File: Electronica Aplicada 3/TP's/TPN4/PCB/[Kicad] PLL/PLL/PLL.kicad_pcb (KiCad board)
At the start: 2 copper layers, 26 parts, among them J1 Alimentacion, J2 SeñalDeReferencia, SW1 SW_SPDT, U1 4017, U2 4046

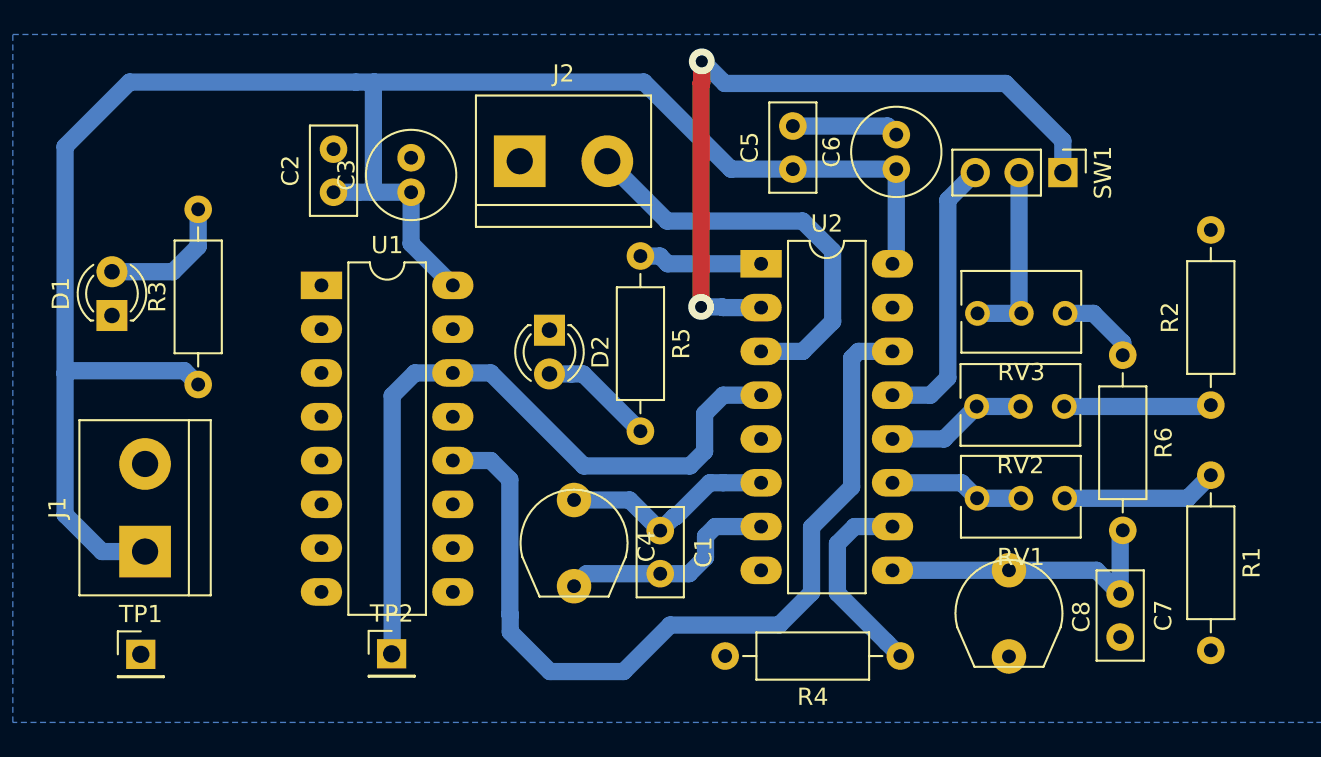
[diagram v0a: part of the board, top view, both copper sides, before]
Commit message: arreglo error PLL y actualizo valores
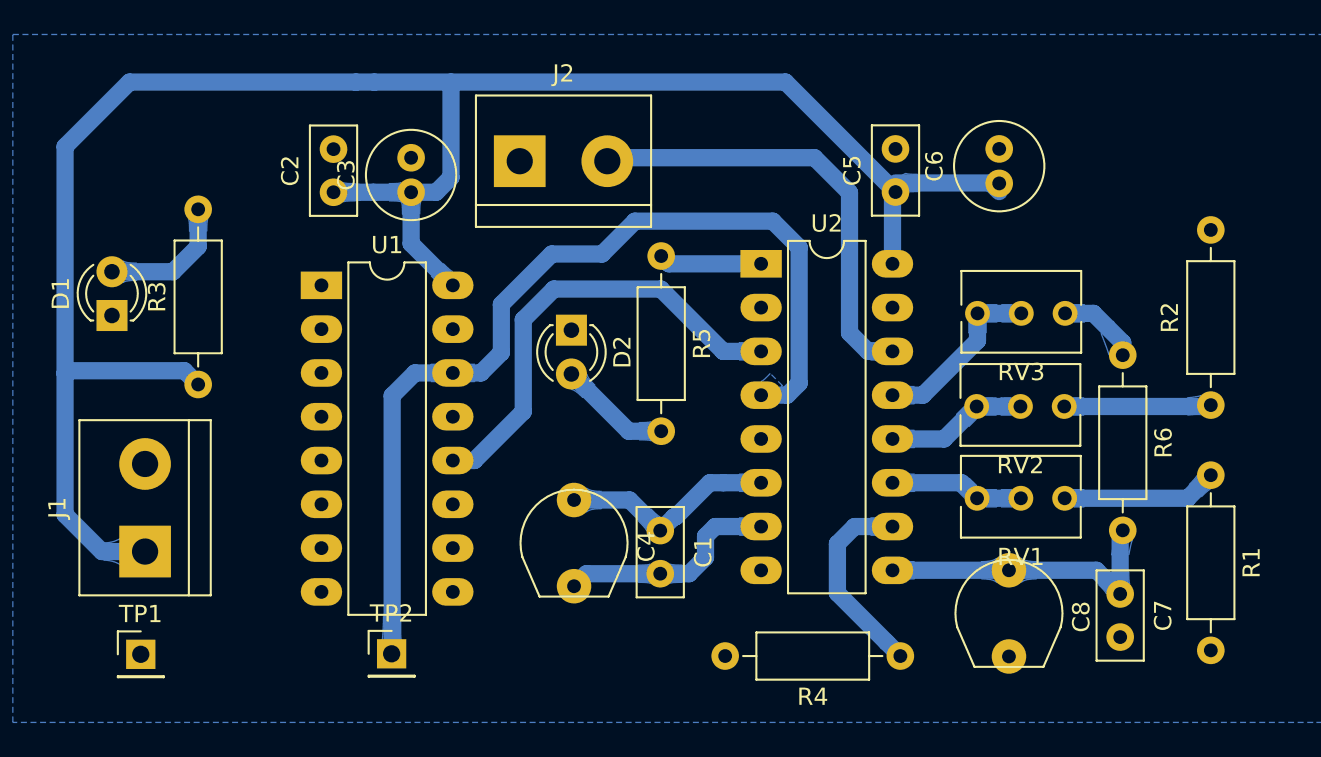
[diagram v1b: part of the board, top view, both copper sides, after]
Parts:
- removed SW1: SW_SPDT, lib_fp:PinHeader_1x03_P2.54mm_Vertical
- C1: value 100n -> 330p
- C4: value 680p -> 0p
- C7, C8: value 680n -> 100n
- moved C5 6.10 mm to (123.4, 31.8)
- moved C6 6.03 mm to (129.5, 31.3)
- moved D2 1.27 mm to (104.6, 39.9)
- moved R5 1.20 mm to (109.9, 35.5)
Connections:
- U2 pad 13: Net-(SW1-Pad3) -> Net-(RV3-Pad1)
- U2 pad 14: Net-(U1-Pad12) -> f_in
- U2 pad 2: Net-(SW1-Pad1) -> (no net)
- U2 pad 3: f_in -> Net-(U1-Pad12)
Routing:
- net Net-(SW1-Pad1): track 42.5 -> 0.00 mm, vias 2 -> 0
- net Net-(U1-Pad12): track 50.0 -> 26.6 mm
- net Net-(SW1-Pad3): track 16.2 -> 0.00 mm
- net Net-(TP2-Pad1): track 41.3 -> 54.6 mm
- net +12V: track 109.7 -> 116.9 mm
- net GND: track 6.21 -> 0.00 mm
- net f_in: track 24.2 -> 26.0 mm
- net Net-(R5-Pad1): track 7.19 -> 5.98 mm

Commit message: Actualizo
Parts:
- added Q1: BC337, lib_fp:TO-92_Inline, F.Cu at (122.0, 31.6)
- added R7: 100, lib_fp:R_Axial_DIN0207_L6.3mm_D2.5mm_P10.16mm_Horizontal, F.Cu at (113.9, 27.8)
- added R8: 10k, lib_fp:R_Axial_DIN0207_L6.3mm_D2.5mm_P10.16mm_Horizontal, F.Cu at (138.5, 27.9)
- moved C5 5.69 mm to (128.7, 34.1)
- moved C6 5.69 mm to (134.7, 33.6)
- moved C2 2.49 mm to (90.8, 29.4), turned to 270 degrees
- moved D2 0.86 mm to (105.5, 39.8)
- moved C4 0.16 mm to (104.9, 52.3)
- moved C8 0.12 mm to (130.0, 56.4)
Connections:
- J2 pad 2: f_in -> generador
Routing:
- net GND: track 0.00 -> 53.6 mm
- net +12V: track 116.9 -> 141.6 mm
- net generador: track 0.00 -> 8.12 mm
- net f_in: track 26.0 -> 19.3 mm
- net Net-(Q1-Pad2): track 0.00 -> 6.28 mm
- net Net-(R4-Pad1): track 11.6 -> 13.1 mm
- net Net-(C1-Pad2): track 13.0 -> 12.3 mm
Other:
- board text added: "+"
- board text added: "+12v"
- board text added: ">3V 15-25 kHz"
- board text added: "GND"
- board text added: "Generador"
- board text added: "SFout"
- board text added: "Salida PLL"

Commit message: Agrego TP3 casi completo, falta conclusion
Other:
- board text added: ">1V|15-25 kHz"
- board text removed: ">3V 15-25 kHz"
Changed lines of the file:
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@@
     (effects (font (size 1 1) (thickness 0.15)))
   )
-  (gr_text ">3V 15-25 kHz" (at 103.886 36.322) (layer F.SilkS)
+  (gr_text ">1V|15-25 kHz" (at 103.886 36.322) (layer F.SilkS)
     (effects (font (size 0.8 0.8) (thickness 0.15)))
   )

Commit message: update
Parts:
- moved C1 76.7 mm to (149.8, 117.0)
- moved R7 76.7 mm to (153.9, 93.3)
- moved C2 76.7 mm to (130.8, 94.9)
- moved C3 76.7 mm to (135.3, 97.3)
- moved C4 76.7 mm to (144.9, 117.8)
- moved C5 76.7 mm to (168.7, 99.6)
- moved C6 76.7 mm to (174.7, 99.1)
- moved C7 76.7 mm to (176.5, 120.7)
- moved C8 76.7 mm to (170.0, 121.9)
- moved D1 76.7 mm to (118.0, 104.5)
- moved D2 76.7 mm to (145.5, 105.3)
- moved J1 76.7 mm to (119.9, 118.2)
- moved J2 76.7 mm to (141.7, 95.5)
- moved Q1 76.7 mm to (162.0, 97.1)
- moved R1 76.7 mm to (181.7, 113.8)
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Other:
- board outline added: 76.5 x 40.5 mm

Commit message: PLL
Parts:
- removed Q1: BC337, lib_fp:TO-92_Inline
- removed R7: 100, lib_fp:R_Axial_DIN0207_L6.3mm_D2.5mm_P10.16mm_Horizontal
- removed R8: 10k, lib_fp:R_Axial_DIN0207_L6.3mm_D2.5mm_P10.16mm_Horizontal
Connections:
- J2 pad 2: generador -> f_in
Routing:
- net generador: track 8.12 -> 0.00 mm
- net f_in: track 19.3 -> 25.8 mm
- net Net-(Q1-Pad2): track 6.28 -> 0.00 mm
- net GND: track 53.6 -> 49.7 mm
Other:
- board text added: "15-25 kHz"
- board text removed: ">1V|15-25 kHz"
